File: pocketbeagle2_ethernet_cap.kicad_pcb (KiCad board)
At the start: 4 copper layers, 35.3 x 55.3 mm, 84 parts, among them J1 1840888-1, P1 PMOD_I2S, P2 PMOD_I2S, Q1 BSS138, Q2 BSS138, Q3 BSS138, U1 PocketBeagle2, U2 DP83867IRPAPR, U3 TPS7A20, U4 TPS7A20, Y1 ECS-2520MV-xxx-xx

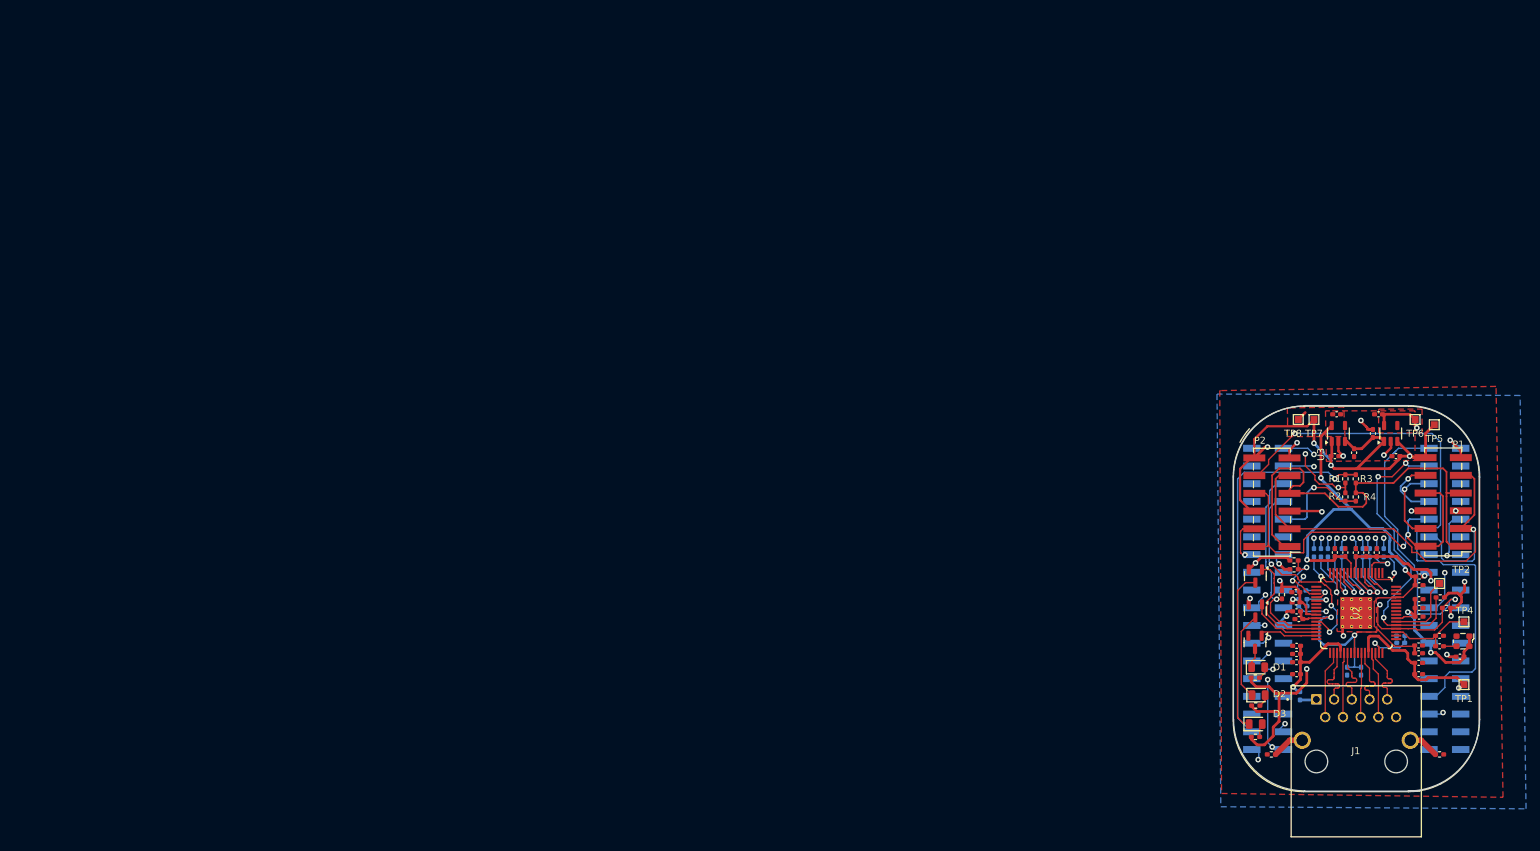
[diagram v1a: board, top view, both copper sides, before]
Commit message: Clear copper for re-spin, sync schematic, add P1/P2 silk
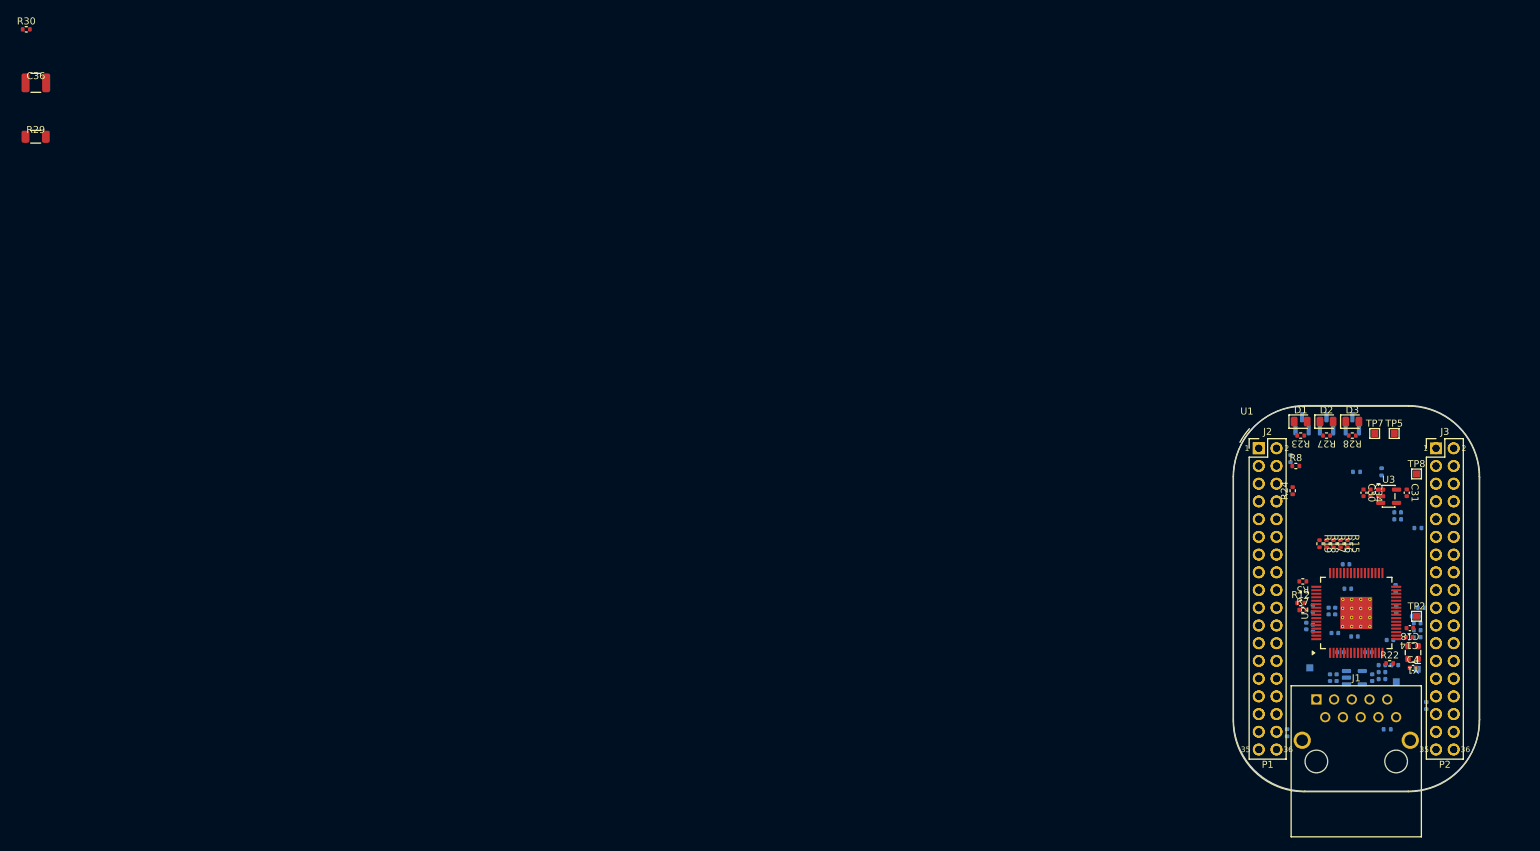
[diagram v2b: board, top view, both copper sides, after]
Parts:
- removed C28: 22pF, Capacitor_SMD:C_0402_1005Metric_Pad0.74x0.62mm_HandSolder
- removed P1, P2: PMOD_I2S, Connector_PinHeader_2.54mm:PinHeader_2x06_P2.54mm_Vertical_SMD
- removed R1, R2, R3, R4: 0R, Resistor_SMD:R_0402_1005Metric_Pad0.72x0.64mm_HandSolder
- removed R25: DNP, Resistor_SMD:R_0402_1005Metric_Pad0.72x0.64mm_HandSolder
- removed R6: 2K49, Resistor_SMD:R_0402_1005Metric_Pad0.72x0.64mm_HandSolder
- added C36: 4n7, KL_Footprints:C_1210, F.Cu at (7.30, 8.74)
- added J2: Header_18x02_2.54mm_2.54mm_Straight, KL_Footprints:18x02_2.54mm_Header, F.Cu at (182.6, 61.1)
- added J3: Header_18x02_2.54mm_2.54mm_Straight, KL_Footprints:18x02_2.54mm_Header, F.Cu at (208.0, 61.1)
- added R30: 5K76, KL_Footprints:R_0402, F.Cu at (5.93, 1.07)
- C1, C10, C13, C2, C3, C35, C5, C6, C9: value 0.1uF -> 100n; footprint Capacitor_SMD:C_0402_1005Metric_Pad0.74x0.62mm_HandSolder -> KL_Footprints:C_0402; moved to B.Cu
- C11, C12, C16, C17, C20, C21, C23, C32, C33, C8: value 1uF -> 1u; footprint Capacitor_SMD:C_0402_1005Metric_Pad0.74x0.62mm_HandSolder -> KL_Footprints:C_0402; moved to B.Cu
- C14: value 27pf -> 27p; footprint Capacitor_SMD:C_0402_1005Metric_Pad0.74x0.62mm_HandSolder -> KL_Footprints:C_0402
- C15, C22, C26: value 10uF -> 10u; footprint Capacitor_SMD:C_0402_1005Metric_Pad0.74x0.62mm_HandSolder -> KL_Footprints:C_0402; moved to B.Cu
- C18: value 27pf -> 22p; footprint Capacitor_SMD:C_0402_1005Metric_Pad0.74x0.62mm_HandSolder -> KL_Footprints:C_0402
- C19, C24, C27: value 0.01uF -> 10n; footprint Capacitor_SMD:C_0402_1005Metric_Pad0.74x0.62mm_HandSolder -> KL_Footprints:C_0402; moved to B.Cu
- C25, C30, C31: value 1uF -> 1u; footprint Capacitor_SMD:C_0402_1005Metric_Pad0.74x0.62mm_HandSolder -> KL_Footprints:C_0402
- C34, C4, C7: value 0.1uF -> 100n; footprint Capacitor_SMD:C_0402_1005Metric_Pad0.74x0.62mm_HandSolder -> KL_Footprints:C_0402
- D1, D2, D3: footprint LED_SMD:LED_0805_2012Metric -> KL_Footprints:LED_0805
- J1: value 1840888-1 -> RJ45_1840888-1; footprint 1840888_1:BEL_1840888-1 -> KL_Footprints:BEL_1840888-1
- Q1, Q2, Q3: value BSS138 -> BSS138LT1G; footprint Package_TO_SOT_SMD:SOT-23 -> KL_Footprints:SOT-23; moved to B.Cu
- R10, R11, R13, R14, R23, R27, R28, R9: footprint Resistor_SMD:R_0402_1005Metric_Pad0.72x0.64mm_HandSolder -> KL_Footprints:R_0402
- R12, R15, R16, R17, R18, R19, R7, R8: footprint Resistor_SMD:R_0402_1005Metric_Pad0.72x0.64mm_HandSolder -> KL_Footprints:R_0402; moved to F.Cu
- R20, R21: value 2.2K -> 2K2; footprint Resistor_SMD:R_0402_1005Metric_Pad0.72x0.64mm_HandSolder -> KL_Footprints:R_0402; moved to B.Cu
- R22: value 11K_1% -> 11K; footprint Resistor_SMD:R_0402_1005Metric_Pad0.72x0.64mm_HandSolder -> KL_Footprints:R_0402; moved to F.Cu
- R24: value 2.2K -> 2K2; footprint Resistor_SMD:R_0402_1005Metric_Pad0.72x0.64mm_HandSolder -> KL_Footprints:R_0402
- R26: footprint Resistor_SMD:R_0402_1005Metric_Pad0.72x0.64mm_HandSolder -> KL_Footprints:R_0402; moved to B.Cu
- R29: value 0R -> 1M; footprint Resistor_SMD:R_0402_1005Metric_Pad0.72x0.64mm_HandSolder -> KL_Footprints:R_1206
- R5: value 5K76 -> 2K49; footprint Resistor_SMD:R_0402_1005Metric_Pad0.72x0.64mm_HandSolder -> KL_Footprints:R_0402
- TP1, TP4, TP6: value TestPoint -> TestPoint_SMD; footprint TestPoint:TestPoint_Pad_1.0x1.0mm -> KL_Footprints:TestPoint_SMD_1.0x1.0mm; moved to B.Cu
- TP2, TP5, TP7, TP8: value TestPoint -> TestPoint_SMD; footprint TestPoint:TestPoint_Pad_1.0x1.0mm -> KL_Footprints:TestPoint_SMD_1.0x1.0mm
- U1: footprint Module:BeagleBoard_PocketBeagle -> KL_Footprints:BeagleBoard_PocketBeagle
- U2: footprint DP83867:PAP0064M_N -> KL_Footprints:HTQFP-64_10x10mm_P0.5mm
- U3: value TPS7A20 -> TPS7A2011PDBVR; footprint Package_TO_SOT_SMD:SOT-23-5 -> KL_Footprints:SOT-23-5
- U4: value TPS7A20 -> TPS7A2025PDBVR; footprint Package_TO_SOT_SMD:SOT-23-5 -> KL_Footprints:SOT-23-5; moved to B.Cu
- Y1: value ECS-2520MV-xxx-xx -> 25M; footprint Oscillator:Oscillator_SMD_ECS_2520MV-xxx-xx-4Pin_2.5x2.0mm -> KL_Footprints:ECS-2520MV
- moved R29 198.0 mm to (7.28, 16.5)
- moved D3 45.5 mm to (196.0, 57.3)
- moved R28 45.4 mm to (196.0, 59.3)
- moved D2 40.4 mm to (192.3, 57.3)
- moved R27 40.0 mm to (192.3, 59.3)
- moved TP6 38.7 mm to (189.9, 92.6)
- moved C33 37.8 mm to (198.8, 94.0), turned to 90 degrees
- moved D1 35.7 mm to (188.6, 57.3)
- moved C32 35.5 mm to (192.8, 94.0), turned to 90 degrees
- moved U4 35.4 mm to (196.3, 94.0), turned to 0 degrees
- moved R23 35.3 mm to (188.6, 59.3)
- moved C35 32.9 mm to (193.8, 94.0), turned to 90 degrees
- moved Q1 32.1 mm to (188.8, 57.6), turned to 90 degrees
- moved Q2 28.7 mm to (192.3, 57.6), turned to 90 degrees
- moved R14 27.6 mm to (186.7, 101.9), turned to 90 degrees
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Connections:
- net /Network/LED0 renamed /network/phy/LED0_PHY_to_Q1
- net /Network/LED1 renamed /network/phy/LED1_PHY_to_Q2
- net /Network/LED2 renamed /network/phy/LED2_PHY_to_Q3
- net /Network/MD0_N renamed /network/phy/MDI0_PHY_RJ45_N
- net /Network/MD0_P renamed /network/phy/MDI0_PHY_RJ45_P
- net /Network/MD1_N renamed /network/phy/MDI1_PHY_RJ45_N
- net /Network/MD1_P renamed /network/phy/MDI1_PHY_RJ45_P
- net /Network/MD2_N renamed /network/phy/MDI2_PHY_RJ45_N
- net /Network/MD2_P renamed /network/phy/MDI2_PHY_RJ45_P
- net /Network/MD3_N renamed /network/phy/MDI3_PHY_RJ45_N
- net /Network/MD3_P renamed /network/phy/MDI3_PHY_RJ45_P
- net /Network/RX_CTRL renamed /network/phy/STRAP_RX_CTRL_PHY
- net /Network/RX_D7 renamed /network/phy/STRAP_RX_D7_PHY
- net /Network/X_IN renamed /network/oscillator/CLK_25M_OSC_to_PHY
- net INT_N/PWRDN_N renamed /INT_PWDN_N_CPU_PHY
- net MDIO0_DIO renamed /MDIO_DIO_CPU_PHY
- net MDIO0_MDC renamed /MDIO_MDC_CPU_PHY
- net RESET_N renamed /RESET_N_CPU_to_PHY
- net RGMII_RD0 renamed /RGMII_RD0_PHY_to_CPU
- net RGMII_RD1 renamed /RGMII_RD1_PHY_to_CPU
- net RGMII_RD2 renamed /RGMII_RD2_PHY_to_CPU
- net RGMII_RD3 renamed /RGMII_RD3_PHY_to_CPU
- net RGMII_RX_CLK renamed /RGMII_RX_CLK_PHY_to_CPU
- net RGMII_RX_CTRL renamed /RGMII_RX_CTRL_PHY_to_CPU
- net RGMII_TD0 renamed /RGMII_TD0_CPU_to_PHY
- net RGMII_TD1 renamed /RGMII_TD1_CPU_to_PHY
- net RGMII_TD2 renamed /RGMII_TD2_CPU_to_PHY
- net RGMII_TD3 renamed /RGMII_TD3_CPU_to_PHY
- net RGMII_TX_CLK renamed /RGMII_TX_CLK_CPU_to_PHY
- net RGMII_TX_CTRL renamed /RGMII_TX_CTRL_CPU_to_PHY
- net VDD_1V1 renamed /VDD_1V1
- net VDD_2V5 renamed /VDD_2V5
- C12 pad 1: VDD_3V3 -> /VDD_3V3
- C16 pad 1: VDD_3V3 -> /VDD_3V3
- C2 pad 1: VDD_3V3 -> /VDD_3V3
- C20 pad 1: VDD_3V3 -> /VDD_3V3
- C22 pad 1: VDD_3V3 -> /VDD_3V3
- C24 pad 1: VDD_3V3 -> /VDD_3V3
- C30 pad 1: GND -> /VDD_3V3
- C30 pad 2: VDD_3V3 -> GND
- C32 pad 1: GND -> /VDD_3V3
- C32 pad 2: VDD_3V3 -> GND
- C34 pad 1: VDD_3V3 -> /VDD_3V3
- C35 pad 1: VDD_3V3 -> /VDD_3V3
- C4 pad 1: VDD_3V3 -> /VDD_3V3
- C6 pad 1: VDD_3V3 -> /VDD_3V3
- C9 pad 1: VDD_3V3 -> /VDD_3V3
- J1 pad 1: Net-(J1-VCC) -> unconnected-(J1-VCC-Pad1)
- J1 pad S1: Net-(J1-SHIELD) -> /network/rj45_connector_port0/CHASSIS
- J1 pad S2: Net-(J1-SHIELD__1) -> /network/rj45_connector_port0/CHASSIS
- R20 pad 2: VDD_3V3 -> /VDD_3V3
- R21 pad 2: VDD_3V3 -> /VDD_3V3
- R23 pad 2: VDD_3V3 -> /VDD_3V3
- R24 pad 1: VDD_3V3 -> /VDD_3V3
- R27 pad 2: VDD_3V3 -> /VDD_3V3
- R28 pad 2: VDD_3V3 -> /VDD_3V3
- R29 pad 2: Net-(J1-SHIELD) -> /network/rj45_connector_port0/CHASSIS
- R5 pad 2: VDD_3V3 -> /VDD_3V3
- TP5 pad 1: VDD_3V3 -> /VDD_3V3
- TP7 pad 1: VDD_3V3 -> /VDD_3V3
- U1 pad 1: unconnected-(U1-VIN-Pad1) -> /io/VIN
- U1 pad 10: MCLK_MCASP -> /io/EXT_REFCLK1
- U1 pad 11: unconnected-(U1-USB1.D+-Pad11) -> /io/USB1_DP
- U1 pad 12: unconnected-(U1-SPI0.MOSI-Pad12) -> /io/SPI0_MOSI
- U1 pad 13: PMOD2.SDIN -> /io/MCASP_AXR12
- U1 pad 14: VDD_3V3 -> /VDD_3V3
- U1 pad 17: unconnected-(U1-AIN.VREF--Pad17) -> /io/AIN_VREF_N
- U1 pad 18: unconnected-(U1-AIN.VREF+-Pad18) -> /io/AIN_VREF_P
- U1 pad 20: unconnected-(U1-GPIO20-Pad20) -> /io/GPIO20
- U1 pad 24: unconnected-(U1-VOUT-Pad24) -> /io/VOUT
- U1 pad 26: unconnected-(U1-I2C2.SDA-Pad26) -> /io/I2C2_SDA
- U1 pad 28: unconnected-(U1-I2C2.SCL-Pad28) -> /io/I2C2_SCL
- U1 pad 29: unconnected-(U1-PRU0.7-Pad29) -> /io/PRU0_7
- U1 pad 3: unconnected-(U1-USB1.DRVVBUS-Pad3) -> /io/USB1_DRVVBUS
- U1 pad 30: unconnected-(U1-UART0.TX-Pad30) -> /io/UART0_TX
- U1 pad 31: unconnected-(U1-PRU0.4-Pad31) -> /io/PRU0_4
- U1 pad 32: unconnected-(U1-UART0.RX-Pad32) -> /io/UART0_RX
- U1 pad 33: MCLK_TOUT -> /io/TIMER_IO1
- U1 pad 36: MCLK_TIN -> /io/TIMER_IO0
- U1 pad 38: unconnected-(U1-GPIO59-Pad38) -> /io/GPIO59
- U1 pad 40: unconnected-(U1-GPIO58-Pad40) -> /io/GPIO58
- U1 pad 41: PMOD1_SDIN -> /io/MCASP2_AXR0
- U1 pad 42: unconnected-(U1-GPIO57-Pad42) -> /io/GPIO57
- U1 pad 43: PMOD1_SDOUT -> /io/MCASP2_AXR1
- U1 pad 44: unconnected-(U1-GPIO60-Pad44) -> /io/GPIO60
- U1 pad 45: LRCK -> /io/MCASP2_AFSX
- U1 pad 47: BCLK -> /io/MCASP2_ACLKX
- U1 pad 48: unconnected-(U1-PWR.BTN-Pad48) -> /io/PWR_BTN
- U1 pad 49: unconnected-(U1-VOUT-Pad49) -> /io/VOUT
- U1 pad 5: unconnected-(U1-USB1.VBUS-Pad5) -> /io/USB1_VBUS
- U1 pad 50: unconnected-(U1-BAT.VIN-Pad50) -> /io/BAT_VIN
- U1 pad 52: unconnected-(U1-BAT.TEMP-Pad52) -> /io/BAT_TEMP
- U1 pad 53: unconnected-(U1-GPIO65-Pad53) -> /io/GPIO65
- U1 pad 54: unconnected-(U1-GPIO47-Pad54) -> /io/GPIO47
- U1 pad 56: unconnected-(U1-GPIO64-Pad56) -> /io/GPIO64
- U1 pad 58: unconnected-(U1-GPIO46-Pad58) -> /io/GPIO46
- U1 pad 59: VDD_3V3 -> /VDD_3V3
- U1 pad 60: unconnected-(U1-GPIO48-Pad60) -> /io/GPIO48
- U1 pad 61: unconnected-(U1-SPI1.MOSI-Pad61) -> /io/SPI1_MOSI
- U1 pad 62: unconnected-(U1-~{RESET}-Pad62) -> /io/NRESET_PB2
- U1 pad 63: unconnected-(U1-SPI1.MISO-Pad63) -> /io/SPI1_MISO
- U1 pad 64: unconnected-(U1-PRU0.6-Pad64) -> /io/PRU0_6
- U1 pad 65: PMOD2.SDOUT -> /io/MCASP_AXR13
- U1 pad 66: unconnected-(U1-PRU0.3-Pad66) -> /io/PRU0_3
- U1 pad 68: unconnected-(U1-PRU0.2-Pad68) -> /io/PRU0_2
- U1 pad 69: unconnected-(U1-GPIO45-Pad69) -> /io/GPIO45
- U1 pad 7: unconnected-(U1-USB1.VIN-Pad7) -> /io/USB1_VIN
- U1 pad 70: unconnected-(U1-PRU0.5-Pad70) -> /io/PRU0_5
- U1 pad 71: unconnected-(U1-AIN5(3.3V)-Pad71) -> /io/AIN5
- U1 pad 72: unconnected-(U1-AIN7(1.8V)-Pad72) -> /io/AIN7
- U1 pad 9: unconnected-(U1-USB1.D--Pad9) -> /io/USB1_DN
- U2 pad 23: VDD_3V3 -> /VDD_3V3
- U2 pad 41: VDD_3V3 -> /VDD_3V3
- U2 pad 57: VDD_3V3 -> /VDD_3V3
- U3 pad 1: VDD_3V3 -> /VDD_3V3
- U3 pad 3: VDD_3V3 -> /VDD_3V3
- U4 pad 1: VDD_3V3 -> /VDD_3V3
- U4 pad 3: VDD_3V3 -> /VDD_3V3
- Y1 pad 1: VDD_3V3 -> /VDD_3V3
- Y1 pad 4: VDD_3V3 -> /VDD_3V3
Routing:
- net VDD_3V3: track 266.6 -> 0.00 mm, vias 13 -> 0
- net /VDD_2V5: track 160.2 -> 0.00 mm, vias 3 -> 0
- net /VDD_1V1: track 99.4 -> 0.00 mm, vias 5 -> 0
- net PMOD2.SDOUT: track 82.0 -> 0.00 mm, vias 1 -> 0
- net /Audio/MCLK: track 68.0 -> 0.00 mm
- net BCLK: track 66.0 -> 0.00 mm, vias 1 -> 0
- net MCLK_TIN: track 59.4 -> 0.00 mm, vias 4 -> 0
- net LRCK: track 59.3 -> 0.00 mm, vias 2 -> 0
- net /MDIO_MDC_CPU_PHY: track 58.0 -> 0.00 mm, vias 2 -> 0
- net MCLK_TOUT: track 55.1 -> 0.00 mm, vias 1 -> 0
- net /RGMII_TX_CLK_CPU_to_PHY: track 49.4 -> 0.00 mm, vias 2 -> 0
- net /MDIO_DIO_CPU_PHY: track 44.8 -> 0.00 mm, vias 3 -> 0
- net GND: track 37.4 -> 0.00 mm, vias 14 -> 0
- net /RGMII_RX_CLK_PHY_to_CPU: track 34.2 -> 0.00 mm, vias 2 -> 0
- net /RGMII_TD1_CPU_to_PHY: track 32.2 -> 0.00 mm, vias 2 -> 0
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- removed copper zone on F.Cu, net /VDD_1V1
- removed copper zone on F.Cu, net /VDD_2V5
- removed copper zone on B.Cu, net GND
- removed copper zone on F.Cu, net GND
- removed copper zone on In1.Cu, net GND
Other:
- outline, holes or cut-outs redrawn
- board text added: "1"
- board text added: "2"
- board text added: "35"
- board text added: "36"
- board text added: "P1"
- board text added: "P2"

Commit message: Route length-matched RGMII, MDI, LEDs and control nets
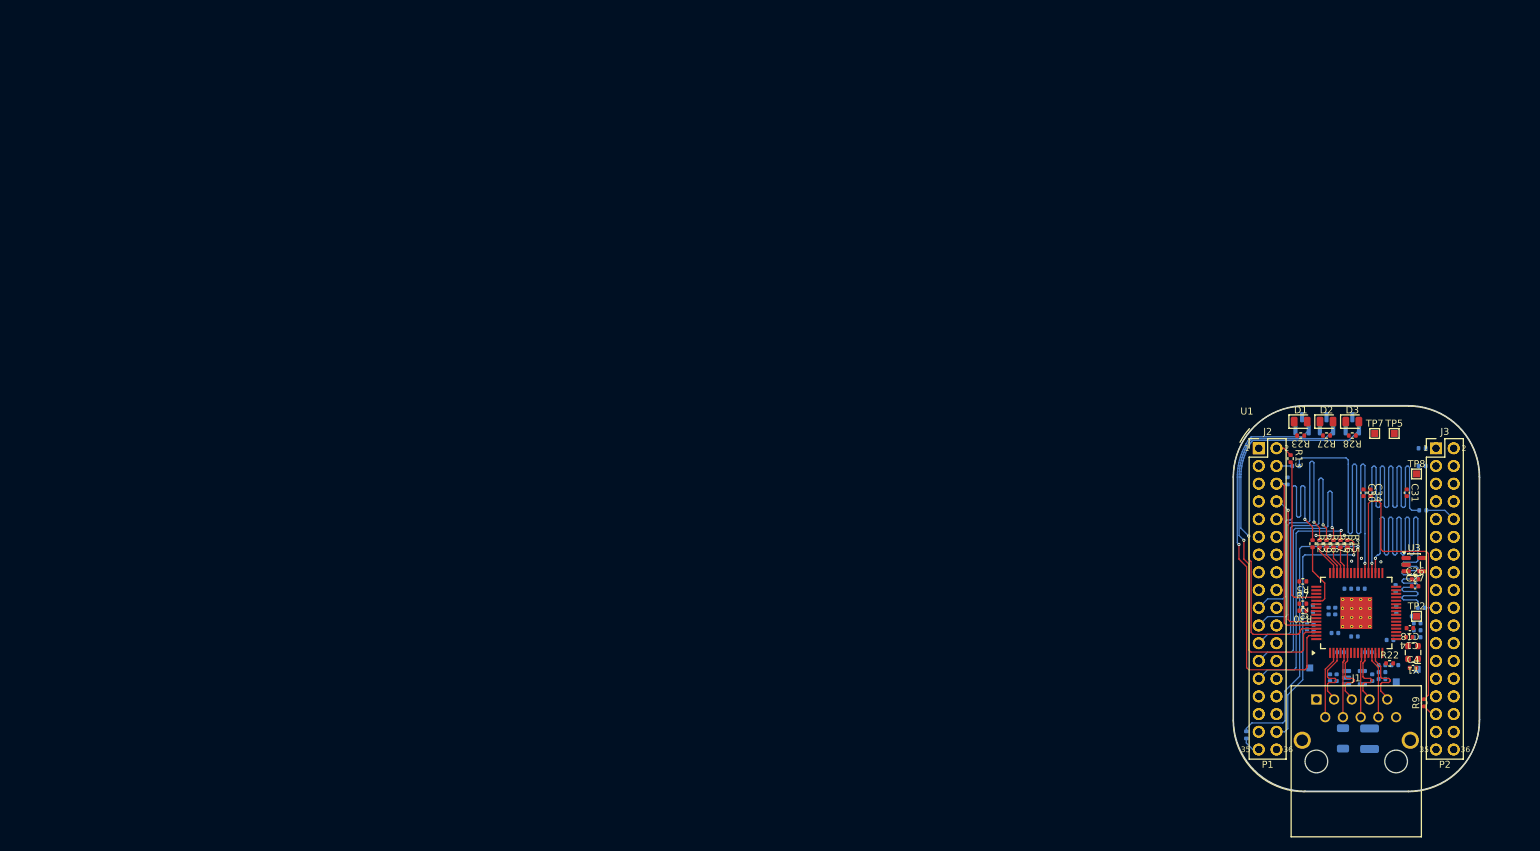
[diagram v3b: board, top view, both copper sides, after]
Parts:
- removed R26: 0R, KL_Footprints:R_0402
- C26, C27, R13, R9: moved to F.Cu
- C36, R24, R29, R8: moved to B.Cu
- moved C36 213.0 mm to (198.5, 102.8), turned to -90 degrees
- moved R29 206.3 mm to (194.7, 102.7), turned to -90 degrees
- moved R30 201.1 mm to (188.9, 84.4), turned to 180 degrees
- moved U3 10.5 mm to (204.8, 77.8)
- moved R20 9.99 mm to (206.0, 61.1)
- moved C26 9.92 mm to (205.0, 79.9)
- moved C27 9.92 mm to (205.0, 80.9)
- moved R12 8.67 mm to (190.3, 74.8), turned to -90 degrees
- moved R21 5.86 mm to (206.0, 63.7), turned to 180 degrees
- moved R14 5.86 mm to (180.8, 102.2)
- moved C6 4.13 mm to (197.3, 81.2)
- moved R10 2.63 mm to (206.1, 70.0)
- moved R24 1.59 mm to (186.7, 65.8), turned to -90 degrees
- moved R7 0.90 mm to (188.9, 83.4)
- moved R9 0.50 mm to (206.3, 97.6)
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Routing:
- net Net-(U2-TX_D3): track 0.00 -> 88.0 mm, vias 0 -> 1
- net Net-(U2-TX_D2): track 0.00 -> 73.5 mm, vias 0 -> 1
- net Net-(U2-TX_D0): track 0.00 -> 65.6 mm, vias 0 -> 1
- net /network/phy/LED0_PHY_to_Q1: track 0.00 -> 57.4 mm, vias 0 -> 1
- net /network/phy/LED1_PHY_to_Q2: track 0.00 -> 55.7 mm, vias 0 -> 1
- net /network/phy/LED2_PHY_to_Q3: track 0.00 -> 54.2 mm, vias 0 -> 1
- net Net-(U2-TX_D1): track 0.00 -> 46.8 mm
- net Net-(U2-GTX_CLK): track 0.00 -> 44.2 mm, vias 0 -> 1
- net /RGMII_RD3_PHY_to_CPU: track 0.00 -> 41.6 mm, vias 0 -> 1
- net /RGMII_RD2_PHY_to_CPU: track 0.00 -> 40.5 mm, vias 0 -> 1
- net /RGMII_RD1_PHY_to_CPU: track 0.00 -> 40.4 mm, vias 0 -> 1
- net /RGMII_RX_CTRL_PHY_to_CPU: track 0.00 -> 39.4 mm, vias 0 -> 1
- net /RGMII_RX_CLK_PHY_to_CPU: track 0.00 -> 37.6 mm, vias 0 -> 1
- net /RGMII_RD0_PHY_to_CPU: track 0.00 -> 33.3 mm, vias 0 -> 1
- net /INT_PWDN_N_CPU_PHY: track 0.00 -> 27.2 mm
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- added copper zone on In1.Cu, net /network/rj45_connector_port0/CHASSIS
- added copper zone on In2.Cu, net /network/rj45_connector_port0/CHASSIS
- added copper zone on In1.Cu, net GND
- added copper zone on In2.Cu, net GND

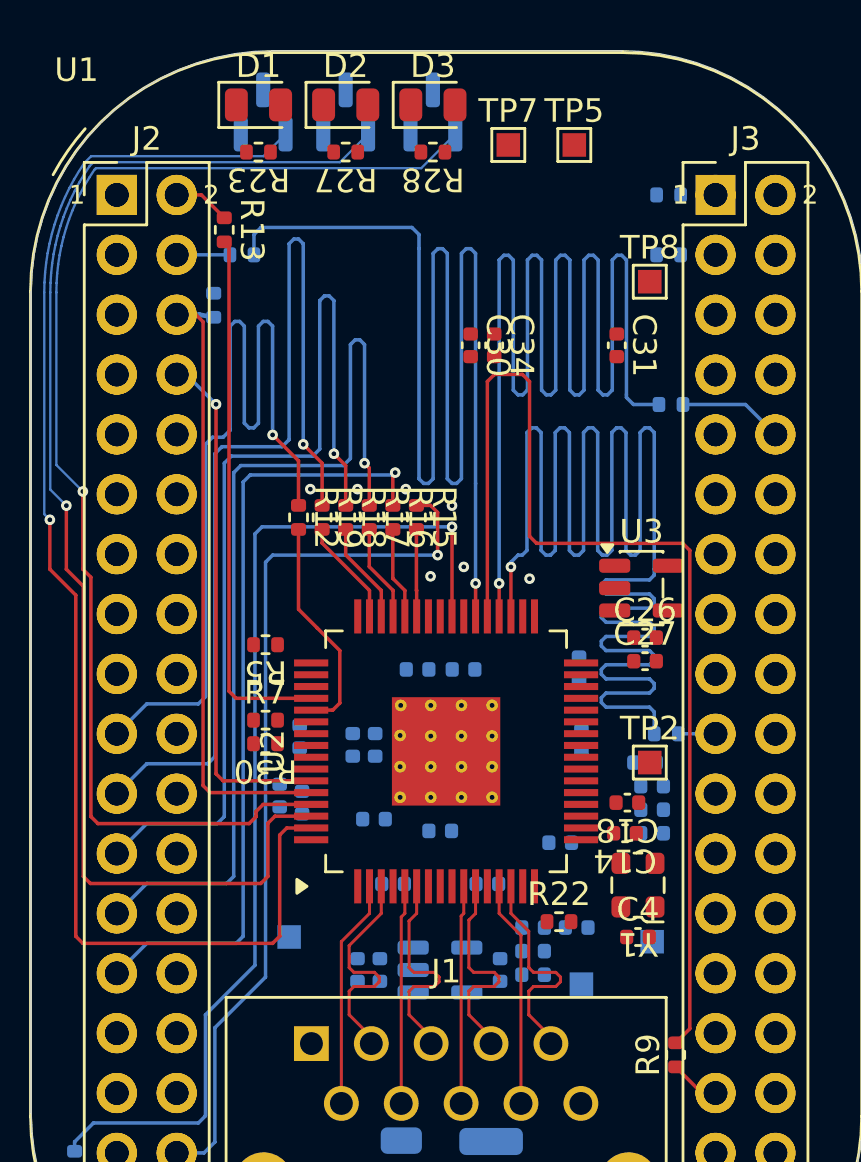
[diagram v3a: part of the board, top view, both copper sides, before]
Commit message: Route power distribution, decoupling and strap resistors
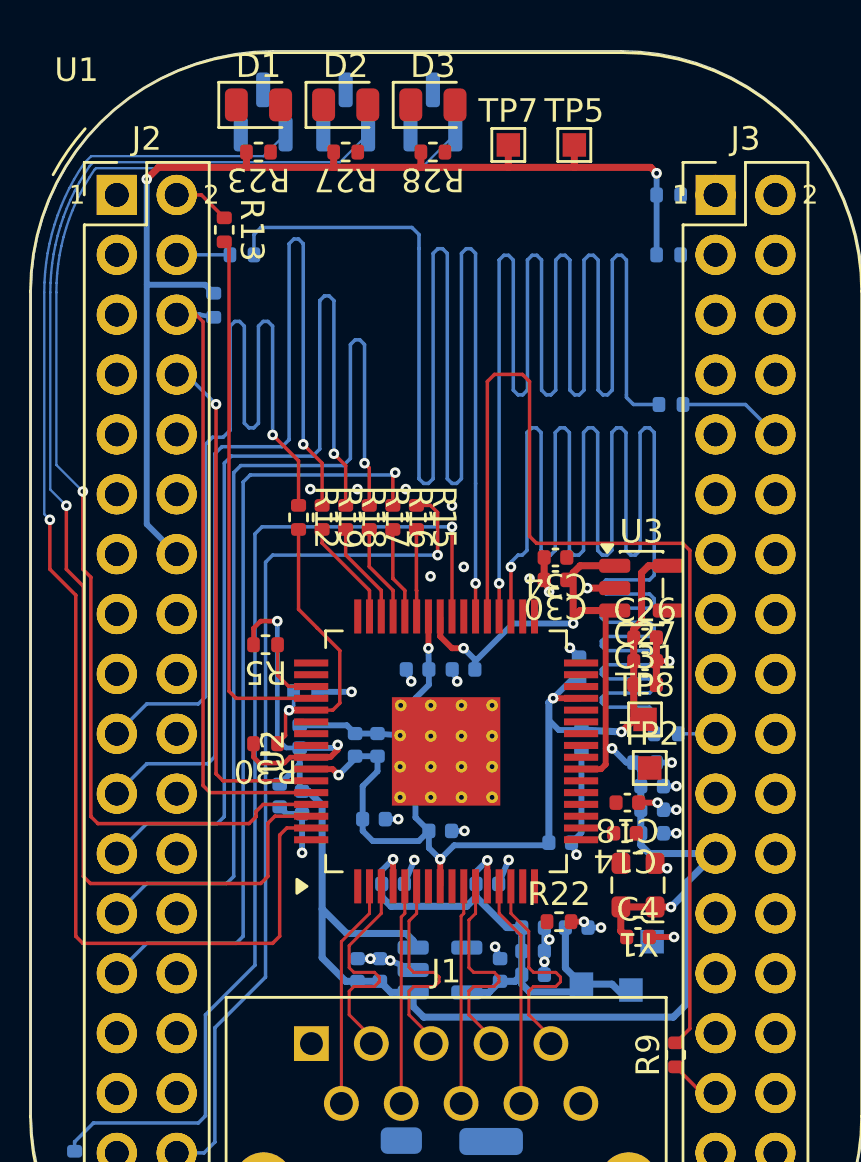
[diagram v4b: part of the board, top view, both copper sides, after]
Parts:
- R7: moved to B.Cu
- moved TP8 18.6 mm to (205.0, 83.4)
- moved TP6 14.7 mm to (204.4, 94.8)
- moved C31 14.4 mm to (205.0, 81.9), turned to 0 degrees
- moved C30 10.6 mm to (201.2, 77.5), turned to 180 degrees
- moved C34 9.37 mm to (201.2, 76.5), turned to 180 degrees
- moved R7 2.08 mm to (190.6, 82.2), turned to 180 degrees
- moved TP2 0.23 mm to (205.2, 85.4)
- moved C25 0.10 mm to (193.7, 84.5)
- moved C3 0.10 mm to (192.7, 84.5)
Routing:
- net /VDD_3V3: track 0.00 -> 136.9 mm, vias 0 -> 8
- net /VDD_1V1: track 0.00 -> 47.4 mm, vias 0 -> 5
- net GND: track 0.00 -> 35.2 mm, vias 7 -> 34
- net /VDD_2V5: track 0.00 -> 25.0 mm, vias 0 -> 2
- net /network/phy/STRAP_RX_CTRL_PHY: track 9.43 -> 12.8 mm, vias 0 -> 1
- net /network/phy/STRAP_RX_D7_PHY: track 0.00 -> 2.92 mm

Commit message: Route MDIO, clock, LEDs, chassis and second 3V3 feed
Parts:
- C18: moved to B.Cu
- moved C18 0.91 mm to (203.3, 87.0), turned to -90 degrees
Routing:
- net /MDIO_MDC_CPU_PHY: track 0.00 -> 42.1 mm, vias 0 -> 1
- net /VDD_3V3: track 136.9 -> 176.1 mm, vias 8 -> 9
- net /MDIO_DIO_CPU_PHY: track 0.00 -> 36.1 mm, vias 0 -> 1
- net /network/rj45_connector_port0/CHASSIS: track 0.00 -> 16.7 mm
- net /network/oscillator/CLK_25M_OSC_to_PHY: track 0.00 -> 9.34 mm, vias 0 -> 1
- net GND: track 35.2 -> 39.0 mm, vias 34 -> 35
- net Net-(U2-CLK_OUT): track 0.00 -> 3.04 mm
- net Net-(D1-K): track 0.00 -> 2.63 mm, vias 0 -> 1
- net Net-(D3-K): track 0.00 -> 2.55 mm, vias 0 -> 1
- net Net-(D2-K): track 0.00 -> 2.55 mm, vias 0 -> 1
- net Net-(D3-A): track 0.00 -> 2.18 mm
- net Net-(D2-A): track 0.00 -> 2.18 mm
- net Net-(D1-A): track 0.00 -> 2.18 mm
- net Net-(U2-RBIAS): track 0.00 -> 2.12 mm
- net Net-(Y1-OUT): track 0.00 -> 1.55 mm
